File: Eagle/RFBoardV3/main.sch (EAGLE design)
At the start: 24 parts, among them Q1 8/16/20MHz, U1 ATMEGA328

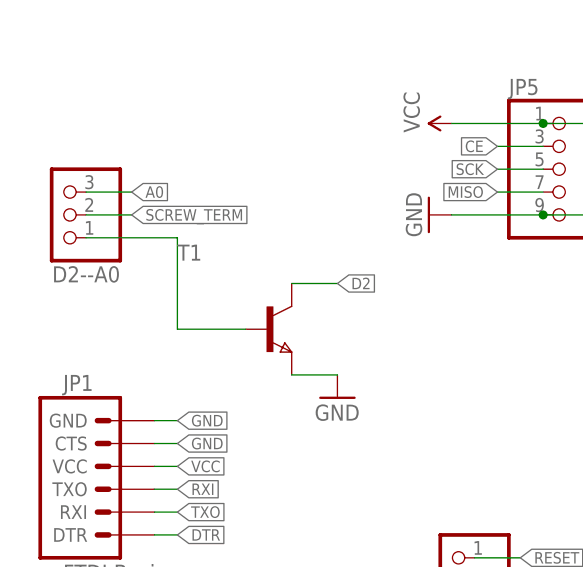
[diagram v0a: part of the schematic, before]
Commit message: Reasonator to top, and added 10k resistor
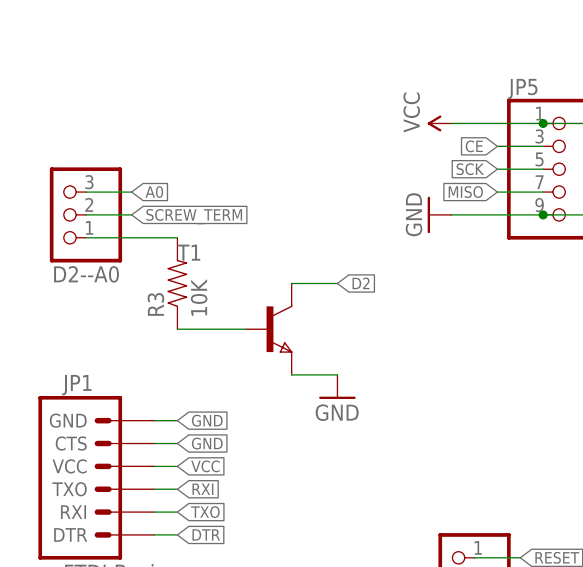
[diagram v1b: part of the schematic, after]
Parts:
- added R3: 10K, SparkFun:RESISTOR0603-RES
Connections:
- new net N$6: R3.1, T1.B
- net N$3: now also R3.2; no longer T1.B
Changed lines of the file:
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@@
 <part name="T1" library="zetex" deviceset="NPNSOT323" device=""/>
 <part name="GND9" library="SparkFun" deviceset="GND" device=""/>
+<part name="R3" library="SparkFun" deviceset="RESISTOR" device="0603-RES" value="10K"/>
 </parts>
 <sheets>
@@
 <instance part="T1" gate="A" x="40.64" y="101.6"/>
 <instance part="GND9" gate="1" x="48.26" y="93.98"/>
+<instance part="R3" gate="G$1" x="30.48" y="106.68" rot="R90"/>
 </instances>
 <busses>
@@
 <pinref part="D2--A0" gate="A" pin="1"/>
 <wire x1="20.32" y1="111.76" x2="30.48" y2="111.76" width="0.1524" layer="91"/>
-<wire x1="30.48" y1="111.76" x2="30.48" y2="101.6" width="0.1524" layer="91"/>
+<pinref part="R3" gate="G$1" pin="2"/>
+</segment>
+</net>
+<net name="N$6" class="0">
+<segment>
 <pinref part="T1" gate="A" pin="B"/>
 <wire x1="30.48" y1="101.6" x2="38.1" y2="101.6" width="0.1524" layer="91"/>
-</segment>
-</net>
+<pinref part="R3" gate="G$1" pin="1"/>
+</segment>
+</net>

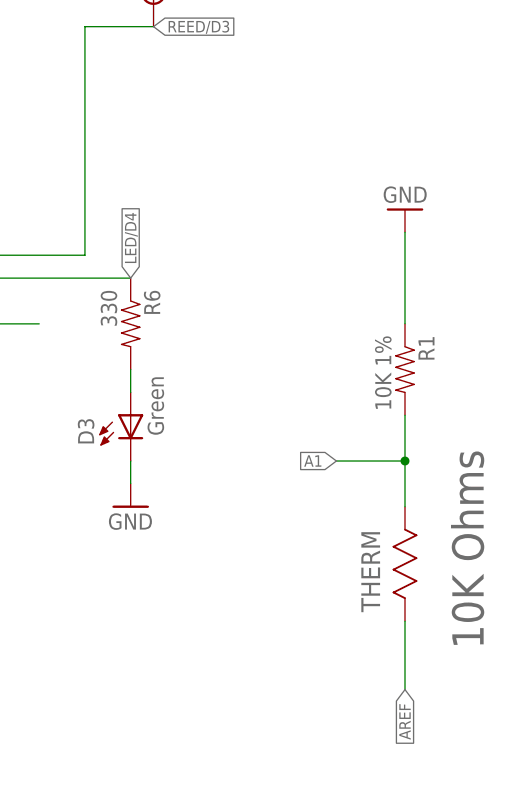
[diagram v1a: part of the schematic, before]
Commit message: Reversed thermister and resistor
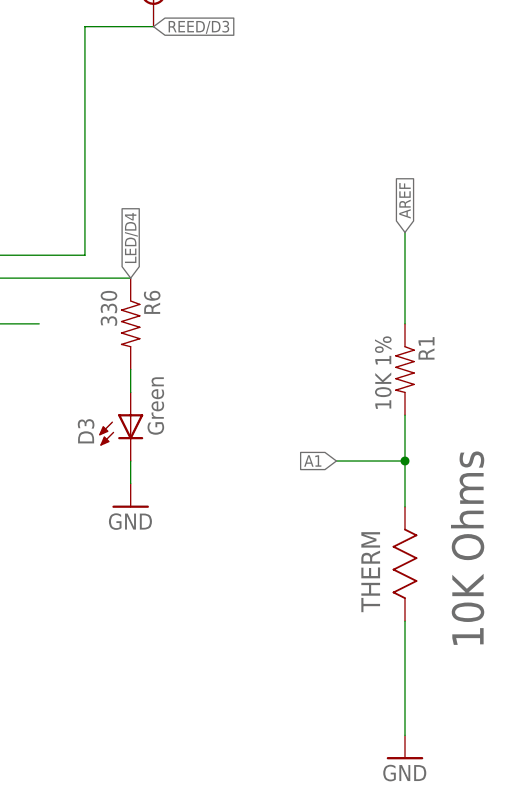
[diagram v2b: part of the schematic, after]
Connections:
- net AREF: now also R1.1; no longer THERM.2
- net GND: now also THERM.2; no longer R1.1
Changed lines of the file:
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@@
 <?xml version="1.0" encoding="utf-8"?>
 <!DOCTYPE eagle SYSTEM "eagle.dtd">
-<eagle version="7.1.0">
+<eagle version="7.2.0">
 <drawing>
 <settings>
@@
 <instance part="THERM" gate="A" x="256.54" y="83.82" rot="R90"/>
 <instance part="D2--A0" gate="A" x="17.78" y="114.3" rot="R180"/>
-<instance part="GND2" gate="1" x="256.54" y="129.54" rot="R180"/>
+<instance part="GND2" gate="1" x="256.54" y="68.58"/>
 <instance part="JP5" gate="A" x="73.66" y="119.38"/>
 <instance part="P+3" gate="G$1" x="60.96" y="124.46" rot="R90"/>
@@
 </segment>
 <segment>
-<pinref part="R1" gate="G$1" pin="1"/>
-<wire x1="256.54" y1="116.84" x2="256.54" y2="127" width="0.1524" layer="91"/>
-<pinref part="GND2" gate="1" pin="GND"/>
-</segment>
-<segment>
 <pinref part="GND6" gate="1" pin="GND"/>
 <pinref part="JP5" gate="A" pin="9"/>
@@
 <pinref part="GND9" gate="1" pin="GND"/>
 <wire x1="43.18" y1="96.52" x2="48.26" y2="96.52" width="0.1524" layer="91"/>
+</segment>
+<segment>
+<pinref part="THERM" gate="A" pin="2"/>
+<pinref part="GND2" gate="1" pin="GND"/>
+<wire x1="256.54" y1="83.82" x2="256.54" y2="71.12" width="0.1524" layer="91"/>
 </segment>
 </net>
@@
 </segment>
 <segment>
-<pinref part="THERM" gate="A" pin="2"/>
-<wire x1="256.54" y1="83.82" x2="256.54" y2="76.2" width="0.1524" layer="91"/>
-<label x="256.54" y="76.2" size="1.27" layer="95" rot="R270" xref="yes"/>
+<label x="256.54" y="127" size="1.27" layer="95" rot="R90" xref="yes"/>
+<pinref part="R1" gate="G$1" pin="1"/>
+<wire x1="256.54" y1="116.84" x2="256.54" y2="127" width="0.1524" layer="91"/>
 </segment>
 </net>

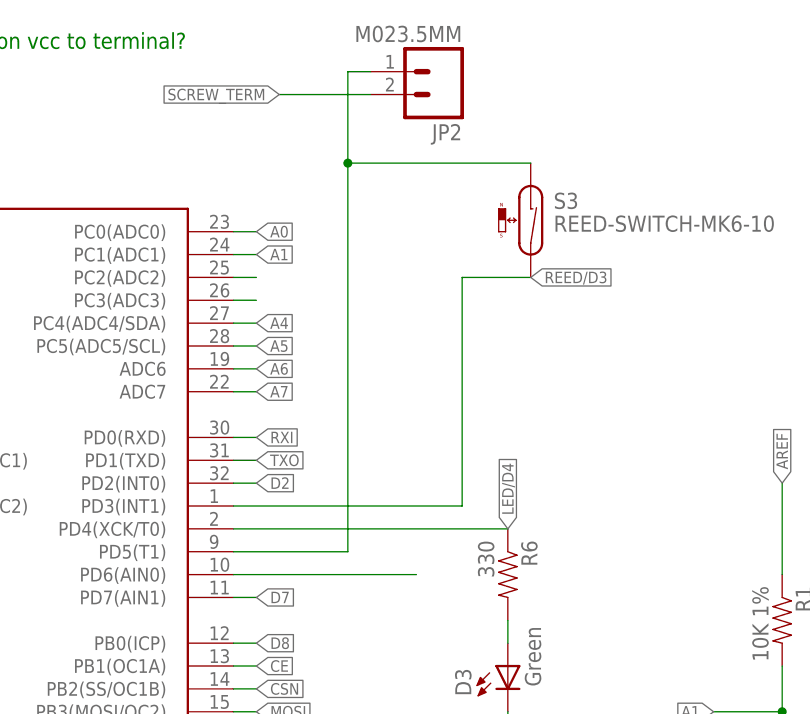
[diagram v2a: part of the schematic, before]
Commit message: Changed reed/term to OR instead of AND
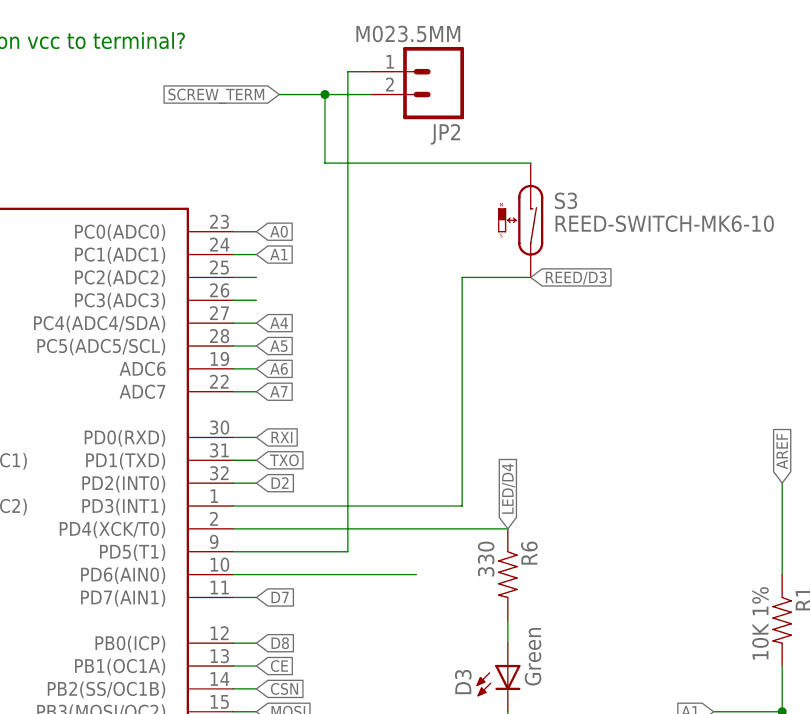
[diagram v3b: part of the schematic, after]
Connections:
- net D5: no longer S3.1
- net SCREW_TERM: now also S3.1
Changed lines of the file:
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@@
 <?xml version="1.0" encoding="utf-8"?>
 <!DOCTYPE eagle SYSTEM "eagle.dtd">
-<eagle version="7.2.0">
+<eagle version="7.1.0">
 <drawing>
 <settings>
@@
 <segment>
 <pinref part="JP2" gate="G$1" pin="2"/>
-<wire x1="210.82" y1="170.18" x2="200.66" y2="170.18" width="0.1524" layer="91"/>
+<wire x1="210.82" y1="170.18" x2="205.74" y2="170.18" width="0.1524" layer="91"/>
 <label x="200.66" y="170.18" size="1.27" layer="95" rot="R180" xref="yes"/>
+<junction x="205.74" y="170.18"/>
+<wire x1="205.74" y1="170.18" x2="200.66" y2="170.18" width="0.1524" layer="91"/>
+<pinref part="S3" gate="G$1" pin="1"/>
+<wire x1="228.6" y1="162.56" x2="205.74" y2="162.56" width="0.1524" layer="91"/>
+<wire x1="205.74" y1="162.56" x2="205.74" y2="170.18" width="0.1524" layer="91"/>
 </segment>
 <segment>
@@
 <pinref part="U1" gate="G$1" pin="PD5(T1)"/>
 <wire x1="195.58" y1="119.38" x2="208.28" y2="119.38" width="0.1524" layer="91"/>
-<wire x1="208.28" y1="119.38" x2="208.28" y2="162.56" width="0.1524" layer="91"/>
+<wire x1="208.28" y1="119.38" x2="208.28" y2="172.72" width="0.1524" layer="91"/>
 <pinref part="JP2" gate="G$1" pin="1"/>
-<wire x1="208.28" y1="162.56" x2="208.28" y2="172.72" width="0.1524" layer="91"/>
 <wire x1="208.28" y1="172.72" x2="210.82" y2="172.72" width="0.1524" layer="91"/>
-<junction x="208.28" y="162.56"/>
-<pinref part="S3" gate="G$1" pin="1"/>
-<wire x1="228.6" y1="162.56" x2="208.28" y2="162.56" width="0.1524" layer="91"/>
-</segment>
-</net>
+</segment>
+</net>
